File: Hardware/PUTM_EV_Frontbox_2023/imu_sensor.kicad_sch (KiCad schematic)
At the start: 4 parts, among them U17 IMS330DHCX

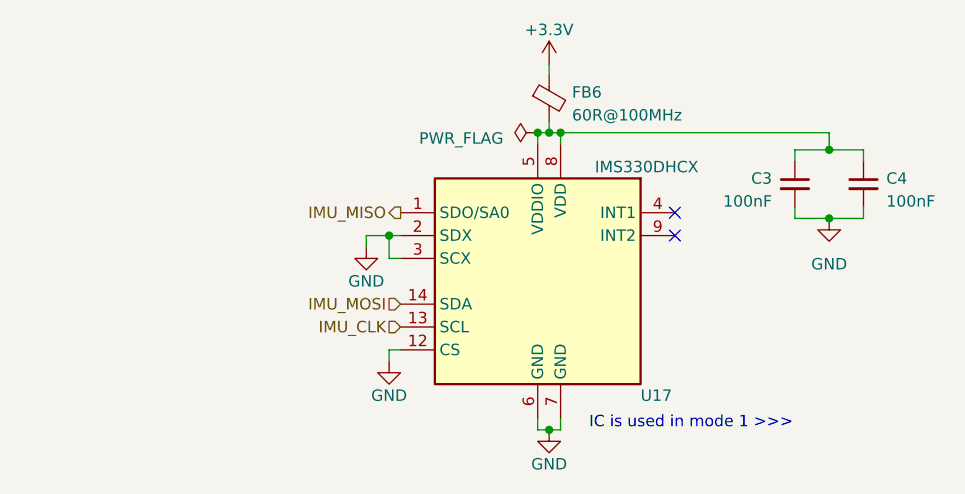
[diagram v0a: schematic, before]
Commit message: Changed mcu pinout
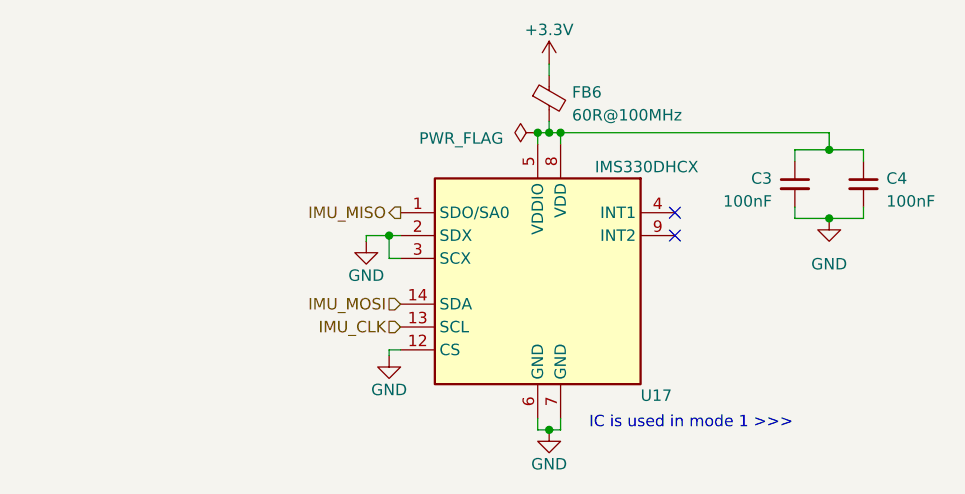
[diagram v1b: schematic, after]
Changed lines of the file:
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@@
     (stroke (width 0) (type default))
   )
-  (wire (pts (xy 92.71 101.6) (xy 92.71 100.33))
+  (wire (pts (xy 92.71 100.965) (xy 92.71 100.33))
     (stroke (width 0) (type default))
   )
@@
     (stroke (width 0) (type default))
   )
-  (wire (pts (xy 90.17 87.63) (xy 90.17 88.9))
+  (wire (pts (xy 90.17 87.63) (xy 90.17 88.265))
     (stroke (width 0) (type default))
   )
@@
     (effects (font (size 1.27 1.27)) (justify right))
   )
-  (symbol (lib_id "power:GND") (at 92.71 101.6 0) (unit 1)
+  (symbol (lib_id "power:GND") (at 92.71 100.965 0) (unit 1)
     (in_bom yes) (on_board yes) (dnp no)
-    (property "Reference" "#PWR027" (at 92.71 107.95 0)
+    (property "Reference" "#PWR027" (at 92.71 107.315 0)
       (effects (font (size 1.27 1.27)) hide)
     )
-    (property "Value" "GND" (at 92.71 105.41 0)
+    (property "Value" "GND" (at 92.71 104.775 0)
       (effects (font (size 1.27 1.27)))
     )
-    (property "Footprint" "" (at 92.71 101.6 0)
+    (property "Footprint" "" (at 92.71 100.965 0)
       (effects (font (size 1.27 1.27)) hide)
     )
-    (property "Datasheet" "" (at 92.71 101.6 0)
+    (property "Datasheet" "" (at 92.71 100.965 0)
       (effects (font (size 1.27 1.27)) hide)
     )
@@
     )
   )
-  (symbol (lib_id "power:GND") (at 90.17 88.9 0) (unit 1)
+  (symbol (lib_id "power:GND") (at 90.17 88.265 0) (unit 1)
     (in_bom yes) (on_board yes) (dnp no)
-    (property "Reference" "#PWR025" (at 90.17 95.25 0)
+    (property "Reference" "#PWR025" (at 90.17 94.615 0)
       (effects (font (size 1.27 1.27)) hide)
     )
-    (property "Value" "GND" (at 90.17 92.71 0)
+    (property "Value" "GND" (at 90.17 92.075 0)
       (effects (font (size 1.27 1.27)))
     )
-    (property "Footprint" "" (at 90.17 88.9 0)
+    (property "Footprint" "" (at 90.17 88.265 0)
       (effects (font (size 1.27 1.27)) hide)
     )
-    (property "Datasheet" "" (at 90.17 88.9 0)
+    (property "Datasheet" "" (at 90.17 88.265 0)
       (effects (font (size 1.27 1.27)) hide)
     )

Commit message: routing done
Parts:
- added R68, R75: 10k, Resistor_SMD:R_0603_1608Metric_Pad0.98x0.95mm_HandSolder, symbol Device:R_Small
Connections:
- net +3.3V: now also U17.12 (CS), R68.1, R75.1
- net GND: no longer U17.12 (CS)
- net IMU_CLK renamed IMU_SCL
- net IMU_SCL: now also R75.2
- net IMU_MISO: no longer names the net of U17.1 (SDO/SA0)
- net IMU_MOSI renamed IMU_SDA
- net IMU_SDA: now also R68.2
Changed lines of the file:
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@@
   (junction (at 109.22 76.2) (diameter 0) (color 0 0 0 0)
   )
+  (junction (at 76.2 97.79) (diameter 0) (color 0 0 0 0)
+  )
+  (junction (at 70.485 84.455) (diameter 0) (color 0 0 0 0)
+  )
   (junction (at 141.605 85.725) (diameter 0) (color 0 0 0 0)
   )
   (junction (at 92.71 87.63) (diameter 0) (color 0 0 0 0)
   )
+  (junction (at 64.77 95.25) (diameter 0) (color 0 0 0 0)
+  )
   (junction (at 141.605 78.105) (diameter 0) (color 0 0 0 0)
   )
@@
     (stroke (width 0) (type default))
   )
+  (wire (pts (xy 64.77 87.63) (xy 64.77 84.455))
+    (stroke (width 0) (type default))
+  )
   (wire (pts (xy 145.415 79.375) (xy 145.415 78.105))
     (stroke (width 0) (type default))
   )
+  (wire (pts (xy 76.2 97.79) (xy 93.98 97.79))
+    (stroke (width 0) (type default))
+  )
   (wire (pts (xy 111.76 76.2) (xy 141.605 76.2))
     (stroke (width 0) (type default))
@@
     (stroke (width 0) (type default))
   )
+  (wire (pts (xy 62.865 97.79) (xy 76.2 97.79))
+    (stroke (width 0) (type default))
+  )
   (wire (pts (xy 137.795 78.105) (xy 141.605 78.105))
     (stroke (width 0) (type default))
@@
     (stroke (width 0) (type default))
   )
+  (wire (pts (xy 92.075 100.33) (xy 92.075 103.505))
+    (stroke (width 0) (type default))
+  )
   (wire (pts (xy 109.22 109.22) (xy 110.49 109.22))
     (stroke (width 0) (type default))
   )
+  (wire (pts (xy 64.77 92.71) (xy 64.77 95.25))
+    (stroke (width 0) (type default))
+  )
+  (wire (pts (xy 76.2 87.63) (xy 76.2 84.455))
+    (stroke (width 0) (type default))
+  )
   (wire (pts (xy 141.605 76.2) (xy 141.605 78.105))
     (stroke (width 0) (type default))
@@
     (stroke (width 0) (type default))
   )
+  (wire (pts (xy 64.77 84.455) (xy 70.485 84.455))
+    (stroke (width 0) (type default))
+  )
   (wire (pts (xy 110.49 76.2) (xy 111.76 76.2))
     (stroke (width 0) (type default))
   )
-  (wire (pts (xy 92.71 100.33) (xy 93.98 100.33))
+  (wire (pts (xy 64.77 95.25) (xy 93.98 95.25))
+    (stroke (width 0) (type default))
+  )
+  (wire (pts (xy 62.865 95.25) (xy 64.77 95.25))
     (stroke (width 0) (type default))
   )
@@
     (stroke (width 0) (type default))
   )
+  (wire (pts (xy 93.98 100.33) (xy 92.075 100.33))
+    (stroke (width 0) (type default))
+  )
   (wire (pts (xy 141.605 78.105) (xy 145.415 78.105))
     (stroke (width 0) (type default))
   )
-  (wire (pts (xy 92.71 100.965) (xy 92.71 100.33))
+  (wire (pts (xy 70.485 84.455) (xy 76.2 84.455))
     (stroke (width 0) (type default))
   )
@@
     (stroke (width 0) (type default))
   )
+  (wire (pts (xy 76.2 92.71) (xy 76.2 97.79))
+    (stroke (width 0) (type default))
+  )
   (wire (pts (xy 110.49 68.58) (xy 110.49 69.85))
     (stroke (width 0) (type default))
@@
     (effects (font (size 1.27 1.27)) (justify left bottom))
   )
-  (hierarchical_label "IMU_CLK" (shape input) (at 93.98 97.79 180) (fields_autoplaced)
-    (effects (font (size 1.27 1.27)) (justify right))
-  )
-  (hierarchical_label "IMU_MISO" (shape output) (at 93.98 85.09 180) (fields_autoplaced)
+  (hierarchical_label "IMU_SCL" (shape bidirectional) (at 62.865 97.79 180) (fields_autoplaced)
     (effects (font (size 1.27 1.27)) (justify right))
   )
-  (hierarchical_label "IMU_MOSI" (shape input) (at 93.98 95.25 180) (fields_autoplaced)
+  (hierarchical_label "IMU_SDA" (shape bidirectional) (at 62.865 95.25 180) (fields_autoplaced)
     (effects (font (size 1.27 1.27)) (justify right))
   )
-  (symbol (lib_id "power:GND") (at 92.71 100.965 0) (unit 1)
-    (in_bom yes) (on_board yes) (dnp no)
-    (property "Reference" "#PWR027" (at 92.71 107.315 0)
-      (effects (font (size 1.27 1.27)) hide)
+  (symbol (lib_id "Device:R_Small") (at 76.2 90.17 0) (unit 1)
+    (in_bom yes) (on_board yes) (dnp no) (fields_autoplaced)
+    (property "Reference" "R75" (at 78.74 88.9 0)
+      (effects (font (size 1.27 1.27)) (justify left))
     )
-    (property "Value" "GND" (at 92.71 104.775 0)
-      (effects (font (size 1.27 1.27)))
+    (property "Value" "10k" (at 78.74 91.44 0)
+      (effects (font (size 1.27 1.27)) (justify left))
     )
-    (property "Footprint" "" (at 92.71 100.965 0)
+    (property "Footprint" "Resistor_SMD:R_0603_1608Metric_Pad0.98x0.95mm_HandSolder" (at 76.2 90.17 0)
       (effects (font (size 1.27 1.27)) hide)
     )
-    (property "Datasheet" "" (at 92.71 100.965 0)
+    (property "Datasheet" "~" (at 76.2 90.17 0)
       (effects (font (size 1.27 1.27)) hide)
     )
     (pin "1")
+    (pin "2")
     (instances
       (project "PUTM_EV_Frontbox_2023"
         (path "/b652b05a-4e3d-4ad1-b032-18886abe7d45/fc1ffdcd-7b51-43f2-87c4-9a5d8609cd78"
-          (reference "#PWR027") (unit 1)
+          (reference "R75") (unit 1)
         )
       )
@@
     )
   )
+  (symbol (lib_id "power:+3.3V") (at 70.485 84.455 0) (unit 1)
+    (in_bom yes) (on_board yes) (dnp no)
+    (property "Reference" "#PWR011" (at 70.485 88.265 0)
+      (effects (font (size 1.27 1.27)) hide)
+    )
+    (property "Value" "+3.3V" (at 70.485 80.645 0)
+      (effects (font (size 1.27 1.27)))
+    )
+    (property "Footprint" "" (at 70.485 84.455 0)
+      (effects (font (size 1.27 1.27)) hide)
+    )
+    (property "Datasheet" "" (at 70.485 84.455 0)
+      (effects (font (size 1.27 1.27)) hide)
+    )
+    (pin "1")
+    (instances
+      (project "PUTM_EV_Frontbox_2023"
+        (path "/b652b05a-4e3d-4ad1-b032-18886abe7d45/fc1ffdcd-7b51-43f2-87c4-9a5d8609cd78"
+          (reference "#PWR011") (unit 1)
+        )
+      )
+    )
+  )
   (symbol (lib_id "ISM330DHCX:LSM6DS3") (at 109.22 92.71 0) (unit 1)
     (in_bom yes) (on_board yes) (dnp no)
@@
     )
   )
+  (symbol (lib_id "power:+3.3V") (at 92.075 103.505 180) (unit 1)
+    (in_bom yes) (on_board yes) (dnp no)
+    (property "Reference" "#PWR013" (at 92.075 99.695 0)
+      (effects (font (size 1.27 1.27)) hide)
+    )
+    (property "Value" "+3.3V" (at 92.075 107.315 0)
+      (effects (font (size 1.27 1.27)))
+    )
+    (property "Footprint" "" (at 92.075 103.505 0)
+      (effects (font (size 1.27 1.27)) hide)
+    )
+    (property "Datasheet" "" (at 92.075 103.505 0)
+      (effects (font (size 1.27 1.27)) hide)
+    )
+    (pin "1")
+    (instances
+      (project "PUTM_EV_Frontbox_2023"
+        (path "/b652b05a-4e3d-4ad1-b032-18886abe7d45/fc1ffdcd-7b51-43f2-87c4-9a5d8609cd78"
+          (reference "#PWR013") (unit 1)
+        )
+      )
+    )
+  )
   (symbol (lib_id "power:PWR_FLAG") (at 109.22 76.2 90) (unit 1)
     (in_bom yes) (on_board yes) (dnp no) (fields_autoplaced)
@@
         )
       )
+    )
+  )
+  (symbol (lib_id "Device:R_Small") (at 64.77 90.17 0) (unit 1)
+    (in_bom yes) (on_board yes) (dnp no) (fields_autoplaced)
+    (property "Reference" "R68" (at 67.31 88.9 0)
+      (effects (font (size 1.27 1.27)) (justify left))
+    )
+    (property "Value" "10k" (at 67.31 91.44 0)
+      (effects (font (size 1.27 1.27)) (justify left))
+    )
+    (property "Footprint" "Resistor_SMD:R_0603_1608Metric_Pad0.98x0.95mm_HandSolder" (at 64.77 90.17 0)
+      (effects (font (size 1.27 1.27)) hide)
+    )
+    (property "Datasheet" "~" (at 64.77 90.17 0)
+      (effects (font (size 1.27 1.27)) hide)
+    )
+    (pin "1")
+    (pin "2")
+    (instances
+      (project "PUTM_EV_Frontbox_2023"
+        (path "/b652b05a-4e3d-4ad1-b032-18886abe7d45/fc1ffdcd-7b51-43f2-87c4-9a5d8609cd78"
+          (reference "R68") (unit 1)
+        )
+      )

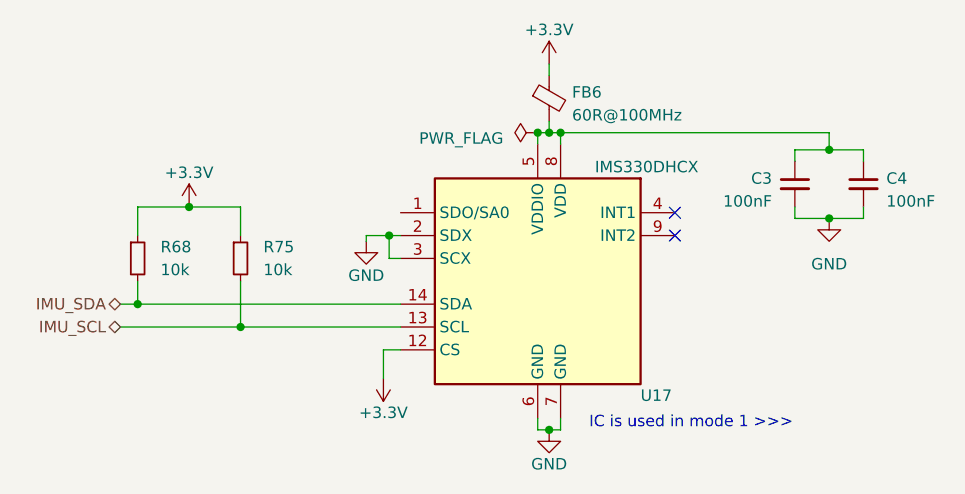
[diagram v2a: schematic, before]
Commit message: Added gearbox temperature sensors on schematic
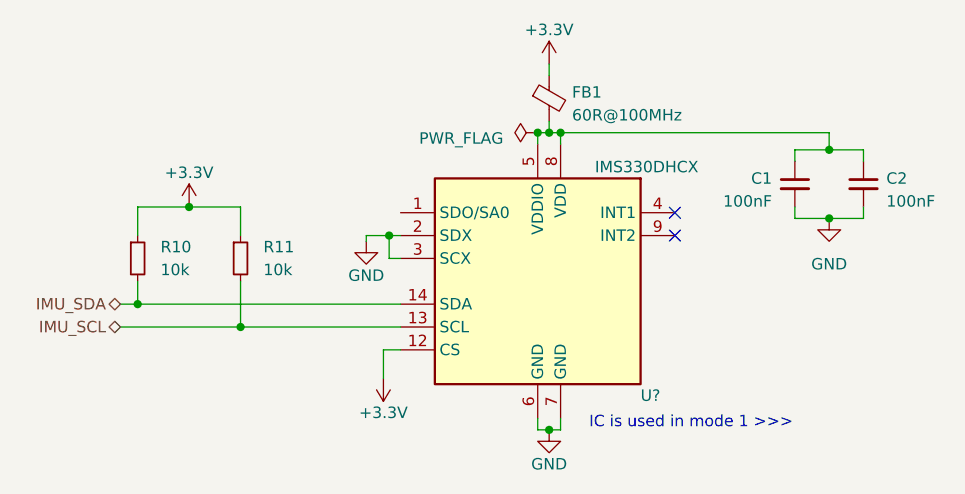
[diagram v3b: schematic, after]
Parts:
- renumbered C3 to C1, C4 to C2, FB6 to FB1, R68 to R10, R75 to R11, U17 to U?
